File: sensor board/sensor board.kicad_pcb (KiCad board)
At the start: 4 copper layers, 21.8 x 18.8 mm, 27 parts, among them IC1 AD5933YRSZ, IC2 MAX86141ENP+, J1 502078-1710, J2 Probe_01_male, J3 Probe_01_male, J4 Probe_01_male, J5 Probe_01_male

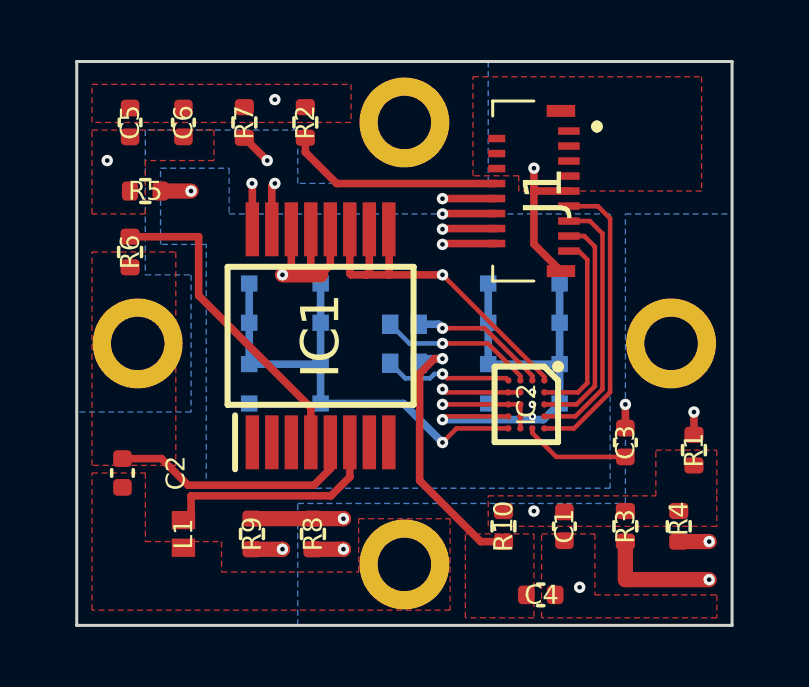
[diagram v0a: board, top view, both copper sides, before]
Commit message: replace LED, changed board layout and created files for production
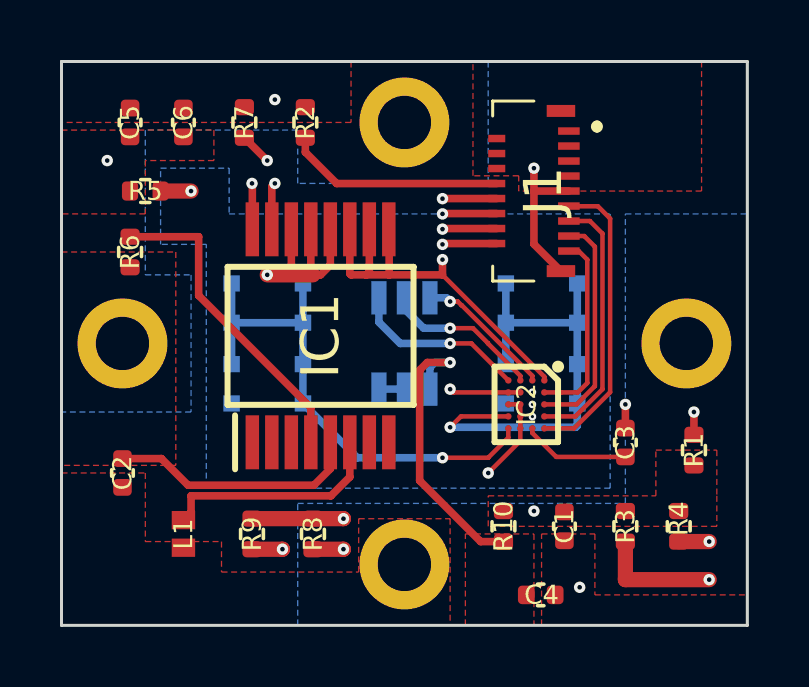
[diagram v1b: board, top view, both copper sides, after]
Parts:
- removed D1: KRTB-EILQ51.3A, Horace:KRTB-EILQ51.3A
- added LED1: 150352M173300, Horace:150352M173300, B.Cu at (141.2, 77.5)
- IC2: value MAX86141ENP+ -> MAX86141ENP+T
- moved D2 0.59 mm to (136.7, 77.5)
- moved D3 0.59 mm to (145.8, 77.5)
- moved J4 0.51 mm to (150.6, 77.5)
- moved J5 0.51 mm to (131.8, 77.5)
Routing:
- net Net-(C4-Pad1): track 9.03 -> 11.6 mm
- net Net-(IC2-PadD1): track 4.34 -> 5.93 mm
- net Net-(D2-Pad1): track 16.1 -> 17.3 mm
- net Net-(D3-Pad1): track 15.4 -> 16.2 mm
- net +3V3: track 23.9 -> 24.6 mm
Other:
- board size 21.8 x 18.8 mm -> 22.9 x 18.8 mm

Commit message: fixed silk labels locations
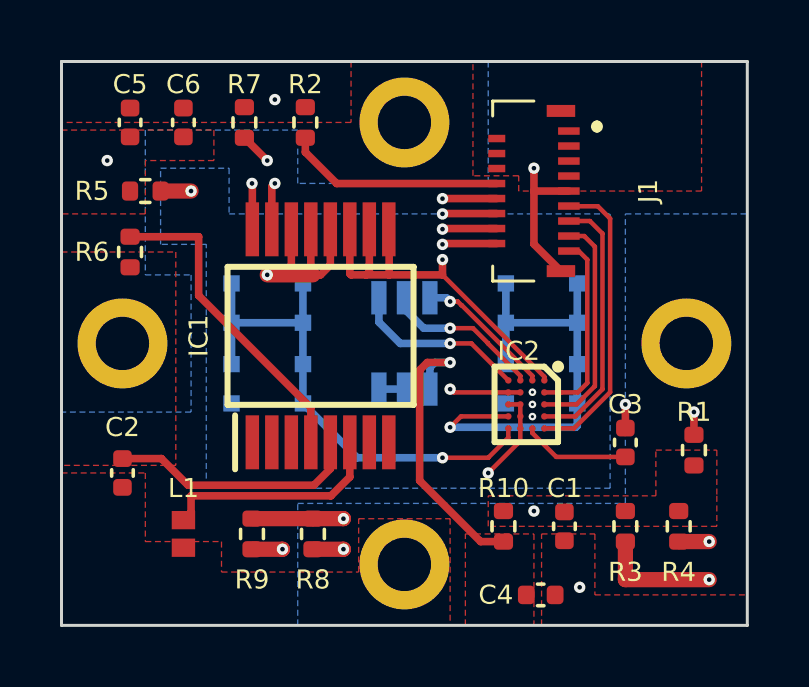
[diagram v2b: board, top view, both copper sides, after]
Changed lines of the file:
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@@
   (page A4)
   (layers
-    (0 F.Cu signal)
-    (1 In1.Cu signal)
-    (2 In2.Cu signal)
-    (31 B.Cu signal)
+    (0 F.Cu signal hide)
+    (1 In1.Cu signal hide)
+    (2 In2.Cu signal hide)
+    (31 B.Cu signal hide)
     (32 B.Adhes user hide)
     (33 F.Adhes user hide)
@@
     (35 F.Paste user hide)
     (36 B.SilkS user hide)
-    (37 F.SilkS user hide)
+    (37 F.SilkS user)
     (38 B.Mask user hide)
-    (39 F.Mask user hide)
+    (39 F.Mask user)
     (40 Dwgs.User user hide)
-    (41 Cmts.User user)
-    (42 Eco1.User user)
-    (43 Eco2.User user)
+    (41 Cmts.User user hide)
+    (42 Eco1.User user hide)
+    (43 Eco2.User user hide)
     (44 Edge.Cuts user)
-    (45 Margin user hide)
+    (45 Margin user)
     (46 B.CrtYd user hide)
     (47 F.CrtYd user)
@@
     (tags resistor)
     (attr smd)
-    (fp_text reference R10 (at 0 0 90) (layer F.SilkS)
+    (fp_text reference R10 (at 1.27 0 180) (layer F.SilkS)
       (effects (font (size 0.635 0.635) (thickness 0.127)))
     )
@@
     (tags resistor)
     (attr smd)
-    (fp_text reference R2 (at 0 0 90) (layer F.SilkS)
+    (fp_text reference R2 (at -1.27 0 180) (layer F.SilkS)
       (effects (font (size 0.635 0.635) (thickness 0.127)))
     )
@@
     (tags resistor)
     (attr smd)
-    (fp_text reference R1 (at 0 0 90) (layer F.SilkS)
+    (fp_text reference R1 (at 1.27 0 180) (layer F.SilkS)
       (effects (font (size 0.635 0.635) (thickness 0.127)))
     )
@@
     (tags resistor)
     (attr smd)
-    (fp_text reference R5 (at 0 0) (layer F.SilkS)
+    (fp_text reference R5 (at 1.778 0) (layer F.SilkS)
       (effects (font (size 0.635 0.635) (thickness 0.127)))
     )
@@
     (tags capacitor)
     (attr smd)
-    (fp_text reference C1 (at 0 0 90) (layer F.SilkS)
+    (fp_text reference C1 (at -1.27 0 180) (layer F.SilkS)
       (effects (font (size 0.635 0.635) (thickness 0.127)))
     )
@@
     (tags capacitor)
     (attr smd)
-    (fp_text reference C3 (at 0 0 90) (layer F.SilkS)
+    (fp_text reference C3 (at 1.27 0 180) (layer F.SilkS)
       (effects (font (size 0.635 0.635) (thickness 0.127)))
     )
@@
     (tags capacitor)
     (attr smd)
-    (fp_text reference C2 (at 0 0 90) (layer F.SilkS)
+    (fp_text reference C2 (at -1.524 0 180) (layer F.SilkS)
       (effects (font (size 0.635 0.635) (thickness 0.1127)))
     )
@@
     (tags capacitor)
     (attr smd)
-    (fp_text reference C4 (at 0.028 0) (layer F.SilkS)
+    (fp_text reference C4 (at -1.496 0) (layer F.SilkS)
       (effects (font (size 0.635 0.635) (thickness 0.127)))
     )
@@
     (tags capacitor)
     (attr smd)
-    (fp_text reference C5 (at 0 0 90) (layer F.SilkS)
+    (fp_text reference C5 (at -1.27 0 180) (layer F.SilkS)
       (effects (font (size 0.635 0.635) (thickness 0.127)))
     )
@@
     (tags capacitor)
     (attr smd)
-    (fp_text reference C6 (at 0 0 90) (layer F.SilkS)
+    (fp_text reference C6 (at -1.27 0 180) (layer F.SilkS)
       (effects (font (size 0.635 0.635) (thickness 0.127)))
     )
@@
     (tags "Integrated Circuit")
     (attr smd)
-    (fp_text reference IC1 (at 0 0 90) (layer F.SilkS)
-      (effects (font (size 1.27 1.27) (thickness 0.254)))
+    (fp_text reference IC1 (at 0 -4.064 90) (layer F.SilkS)
+      (effects (font (size 0.635 0.635) (thickness 0.127)))
     )
     (fp_text value AD5933YRSZ (at 0 0 90) (layer F.SilkS) hide
@@
     (tags "Integrated Circuit")
     (attr smd)
-    (fp_text reference IC2 (at 0 0 90) (layer F.SilkS)
+    (fp_text reference IC2 (at -1.778 0.254 180) (layer F.SilkS)
       (effects (font (size 0.635 0.635) (thickness 0.127)))
     )
@@
     (tags Connector)
     (attr smd)
-    (fp_text reference J1 (at 0 0.313 90) (layer F.SilkS)
-      (effects (font (size 1.27 1.27) (thickness 0.254)))
+    (fp_text reference J1 (at 0 3.81 90) (layer F.SilkS)
+      (effects (font (size 0.635 0.635) (thickness 0.127)))
     )
     (fp_text value 502078-1710 (at 0 0.313 90) (layer F.SilkS) hide
@@
     (tags resistor)
     (attr smd)
-    (fp_text reference R3 (at 0 0 90) (layer F.SilkS)
+    (fp_text reference R3 (at 1.524 0 180) (layer F.SilkS)
       (effects (font (size 0.635 0.635) (thickness 0.127)))
     )
@@
     (tags resistor)
     (attr smd)
-    (fp_text reference R4 (at -0.254 0 90) (layer F.SilkS)
+    (fp_text reference R4 (at 1.524 0 180) (layer F.SilkS)
       (effects (font (size 0.635 0.635) (thickness 0.127)))
     )
@@
     (tags resistor)
     (attr smd)
-    (fp_text reference R7 (at 0 0 90) (layer F.SilkS)
+    (fp_text reference R7 (at -1.27 0 180) (layer F.SilkS)
       (effects (font (size 0.635 0.635) (thickness 0.127)))
     )
@@
     (tags resistor)
     (attr smd)
-    (fp_text reference R8 (at 0 0 90) (layer F.SilkS)
+    (fp_text reference R8 (at -1.524 0 180) (layer F.SilkS)
       (effects (font (size 0.635 0.635) (thickness 0.127)))
     )
@@
     (tags resistor)
     (attr smd)
-    (fp_text reference R9 (at 0 0 90) (layer F.SilkS)
+    (fp_text reference R9 (at -1.524 0 180) (layer F.SilkS)
       (effects (font (size 0.635 0.635) (thickness 0.127)))
     )
@@
     (tags resistor)
     (attr smd)
-    (fp_text reference R6 (at 0 0 90) (layer F.SilkS)
+    (fp_text reference R6 (at 0 -1.27 180) (layer F.SilkS)
       (effects (font (size 0.635 0.635) (thickness 0.127)))
     )
@@
   (module Horace:LQW15DN150M00D (layer F.Cu)
     (at 133.858 83.82 270)
-    (fp_text reference L1 (at 0 0 90) (layer F.SilkS)
+    (fp_text reference L1 (at -1.524 0 180) (layer F.SilkS)
       (effects (font (size 0.635 0.635) (thickness 0.127)))
     )
@@
       (effects (font (size 1 1) (thickness 0.15)) (justify mirror))
     )
-    (fp_text value 150352M173300 (at 0 0 270) (layer B.SilkS)
+    (fp_text value 150352M173300 (at 0 0 270) (layer B.SilkS) hide
       (effects (font (size 1 1) (thickness 0.15)) (justify mirror))
     )
